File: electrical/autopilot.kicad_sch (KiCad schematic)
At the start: 5 parts

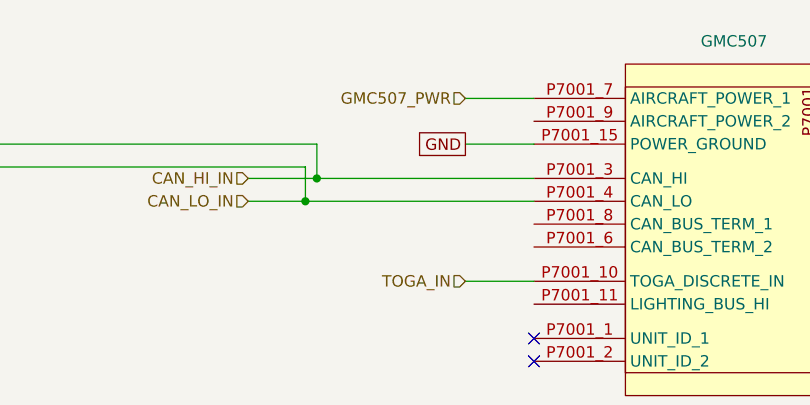
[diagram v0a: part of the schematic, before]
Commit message: Converted to breakers w/GAD 27 instead of VP-X.
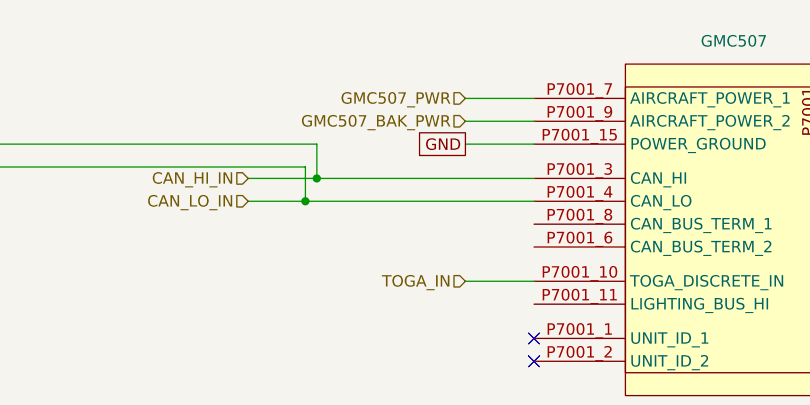
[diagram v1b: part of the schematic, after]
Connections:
- net GMC507_BAK_PWR: now reaches GMC507.P7001_9 (AIRCRAFT_POWER_2)
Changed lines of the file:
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@@
     (title "Autopilot")
     (date "2024-02-13")
-    (rev "0.9.1")
+    (rev "1.0")
     (company "N915SN Angry Bird")
+    (comment 1 "w/Breakers")
   )
   (junction (at 62.23 86.36) (diameter 0) (color 0 0 0 0)
@@
     (stroke (width 0) (type default))
   )
+  (wire (pts (xy 196.85 26.67) (xy 204.47 26.67))
+    (stroke (width 0) (type default))
+  )
   (wire (pts (xy 55.88 25.4) (xy 68.58 25.4))
     (stroke (width 0) (type default))
@@
     (effects (font (size 1.27 1.27)) (justify left))
   )
+  (hierarchical_label "GMC507_BAK_PWR" (shape input) (at 196.85 26.67 180) (fields_autoplaced)
+    (effects (font (size 1.27 1.27)) (justify right))
+  )
   (hierarchical_label "CAN_LO_IN" (shape input) (at 172.72 35.56 180) (fields_autoplaced)

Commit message: Unknown set of changes. Didn't spent time to look
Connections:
- net PITCH_TRIM_1_IN: no longer names the net of GSA28_PITCH.P281_11 (TRIM_IN_1)
- net PITCH_TRIM_1_OUT: no longer names the net of GSA28_PITCH.P281_13 (TRIM_OUT_1)
- net PITCH_TRIM_2_IN: no longer names the net of GSA28_PITCH.P281_12 (TRIM_IN_2)
- net PITCH_TRIM_2_OUT: no longer names the net of GSA28_PITCH.P281_14 (TRIM_OUT_2)
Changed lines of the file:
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@@
     (title "Autopilot")
     (date "2024-02-13")
-    (rev "1.0")
+    (rev "1.0.1")
     (company "N915SN Angry Bird")
     (comment 1 "w/Breakers")
@@
     (stroke (width 0) (type default))
   )
-  (wire (pts (xy 55.88 106.68) (xy 88.9 106.68))
-    (stroke (width 0) (type default))
-  )
   (wire (pts (xy 58.42 185.42) (xy 55.88 185.42))
     (stroke (width 0) (type default))
@@
     (stroke (width 0) (type default))
   )
-  (wire (pts (xy 55.88 104.14) (xy 88.9 104.14))
-    (stroke (width 0) (type default))
-  )
   (wire (pts (xy 74.93 29.21) (xy 180.34 29.21))
     (stroke (width 0) (type default))
@@
     (stroke (width 0) (type default))
   )
-  (wire (pts (xy 55.88 113.03) (xy 88.9 113.03))
-    (stroke (width 0) (type default))
-  )
   (wire (pts (xy 55.88 31.75) (xy 73.66 31.75))
     (stroke (width 0) (type default))
@@
     (stroke (width 0) (type default))
   )
+  (wire (pts (xy 55.88 25.4) (xy 68.58 25.4))
+    (stroke (width 0) (type default))
+  )
+  (wire (pts (xy 74.93 29.21) (xy 74.93 92.71))
+    (stroke (width 0) (type default))
+  )
+  (wire (pts (xy 180.34 33.02) (xy 172.72 33.02))
+    (stroke (width 0) (type default))
+  )
+  (wire (pts (xy 99.06 53.34) (xy 104.14 53.34))
+    (stroke (width 0) (type default))
+  )
+  (wire (pts (xy 73.66 154.94) (xy 55.88 154.94))
+    (stroke (width 0) (type default))
+  )
+  (wire (pts (xy 180.34 33.02) (xy 204.47 33.02))
+    (stroke (width 0) (type default))
+  )
+  (wire (pts (xy 55.88 92.71) (xy 74.93 92.71))
+    (stroke (width 0) (type default))
+  )
+  (wire (pts (xy 62.23 22.86) (xy 68.58 22.86))
+    (stroke (width 0) (type default))
+  )
+  (wire (pts (xy 64.77 116.84) (xy 64.77 53.34))
+    (stroke (width 0) (type default))
+  )
+  (wire (pts (xy 55.88 22.86) (xy 62.23 22.86))
+    (stroke (width 0) (type default))
+  )
+  (wire (pts (xy 196.85 29.21) (xy 204.47 29.21))
+    (stroke (width 0) (type default))
+  )
   (wire (pts (xy 196.85 26.67) (xy 204.47 26.67))
-    (stroke (width 0) (type default))
-  )
-  (wire (pts (xy 55.88 25.4) (xy 68.58 25.4))
-    (stroke (width 0) (type default))
-  )
-  (wire (pts (xy 74.93 29.21) (xy 74.93 92.71))
-    (stroke (width 0) (type default))
-  )
-  (wire (pts (xy 180.34 33.02) (xy 172.72 33.02))
-    (stroke (width 0) (type default))
-  )
-  (wire (pts (xy 99.06 53.34) (xy 104.14 53.34))
-    (stroke (width 0) (type default))
-  )
-  (wire (pts (xy 73.66 154.94) (xy 55.88 154.94))
-    (stroke (width 0) (type default))
-  )
-  (wire (pts (xy 180.34 33.02) (xy 204.47 33.02))
-    (stroke (width 0) (type default))
-  )
-  (wire (pts (xy 55.88 92.71) (xy 74.93 92.71))
-    (stroke (width 0) (type default))
-  )
-  (wire (pts (xy 62.23 22.86) (xy 68.58 22.86))
-    (stroke (width 0) (type default))
-  )
-  (wire (pts (xy 64.77 116.84) (xy 64.77 53.34))
-    (stroke (width 0) (type default))
-  )
-  (wire (pts (xy 55.88 22.86) (xy 62.23 22.86))
-    (stroke (width 0) (type default))
-  )
-  (wire (pts (xy 196.85 29.21) (xy 204.47 29.21))
-    (stroke (width 0) (type default))
-  )
-  (wire (pts (xy 55.88 110.49) (xy 88.9 110.49))
     (stroke (width 0) (type default))
   )
@@
     (effects (font (size 1.27 1.27)) (justify left))
   )
-  (hierarchical_label "PITCH_TRIM_1_IN" (shape bidirectional) (at 88.9 104.14 0) (fields_autoplaced)
-    (effects (font (size 1.27 1.27)) (justify left))
+  (hierarchical_label "CAN_LO_IN" (shape input) (at 172.72 35.56 180) (fields_autoplaced)
+    (effects (font (size 1.27 1.27)) (justify right))
   )
   (hierarchical_label "GMC507_BAK_PWR" (shape input) (at 196.85 26.67 180) (fields_autoplaced)
     (effects (font (size 1.27 1.27)) (justify right))
   )
-  (hierarchical_label "CAN_LO_IN" (shape input) (at 172.72 35.56 180) (fields_autoplaced)
-    (effects (font (size 1.27 1.27)) (justify right))
-  )
-  (hierarchical_label "PITCH_TRIM_2_IN" (shape bidirectional) (at 88.9 106.68 0) (fields_autoplaced)
-    (effects (font (size 1.27 1.27)) (justify left))
-  )
   (hierarchical_label "TOGA_IN" (shape input) (at 196.85 44.45 180) (fields_autoplaced)
     (effects (font (size 1.27 1.27)) (justify right))
   )
-  (hierarchical_label "PITCH_TRIM_1_OUT" (shape bidirectional) (at 88.9 110.49 0) (fields_autoplaced)
-    (effects (font (size 1.27 1.27)) (justify left))
-  )
-  (hierarchical_label "PITCH_TRIM_2_OUT" (shape bidirectional) (at 88.9 113.03 0) (fields_autoplaced)
-    (effects (font (size 1.27 1.27)) (justify left))
-  )
   (hierarchical_label "GND_BUS" (shape input) (at 30.48 200.66 180) (fields_autoplaced)

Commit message: Interim check-in. Not sure what I was doing.
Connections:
- no-connect marks 10 -> 14
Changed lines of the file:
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@@
   (no_connect (at 55.88 62.23))
   (no_connect (at 55.88 59.69))
+  (no_connect (at 55.88 97.79))
   (no_connect (at 204.47 50.8))
+  (no_connect (at 55.88 34.29))
+  (no_connect (at 55.88 100.33))
   (no_connect (at 55.88 123.19))
   (no_connect (at 55.88 64.77))
   (no_connect (at 55.88 57.15))
   (no_connect (at 57.15 187.96))
+  (no_connect (at 55.88 36.83))
   (no_connect (at 55.88 180.34))
   (no_connect (at 55.88 125.73))
@@
     (stroke (width 0) (type default))
   )
+  (text_box "SportAir Wired\n1 CAN H\n2 CAN L\n3 CAN TERM 1\n4 CAN TERM 2\n9 GROUND\n10 POWER\n15 CWS"
+    (at 84.455 97.79 0) (size 16.51 17.145)
+    (stroke (width 0) (type default))
+    (fill (type none))
+    (effects (font (size 1.27 1.27)) (justify left top))
+  )
   (text "Canbus Termination" (at 67.31 160.02 0)

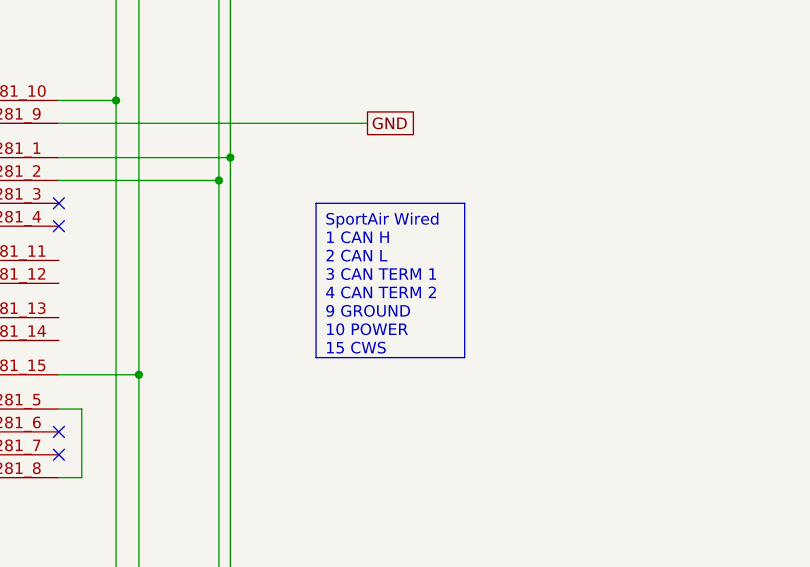
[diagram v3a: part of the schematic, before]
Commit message: Cleaned up power and smoke.
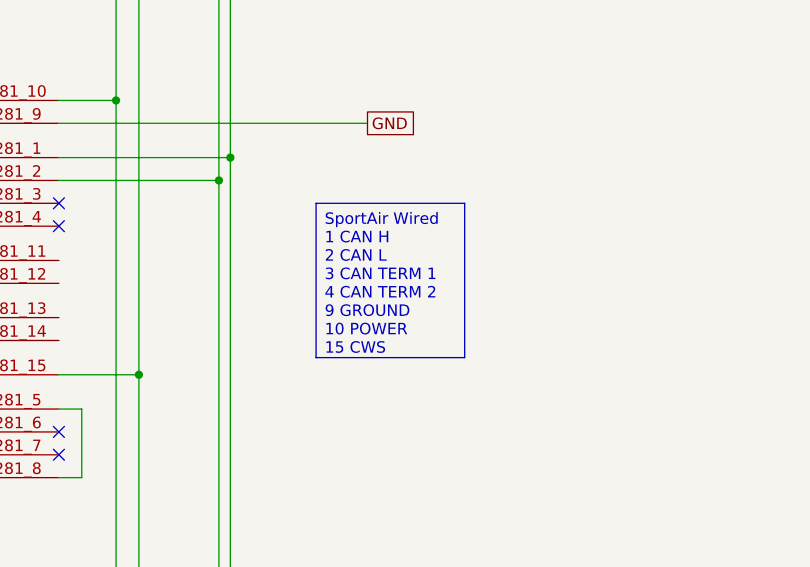
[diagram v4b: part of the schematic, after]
